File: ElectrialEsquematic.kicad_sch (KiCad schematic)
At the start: 8 parts, among them J1 Conn_01x02_Female, U1 RFM95W-915S2, U3 TP4056, U4 DHT11, U5 NHD-C0220BIZ, U6 L7805

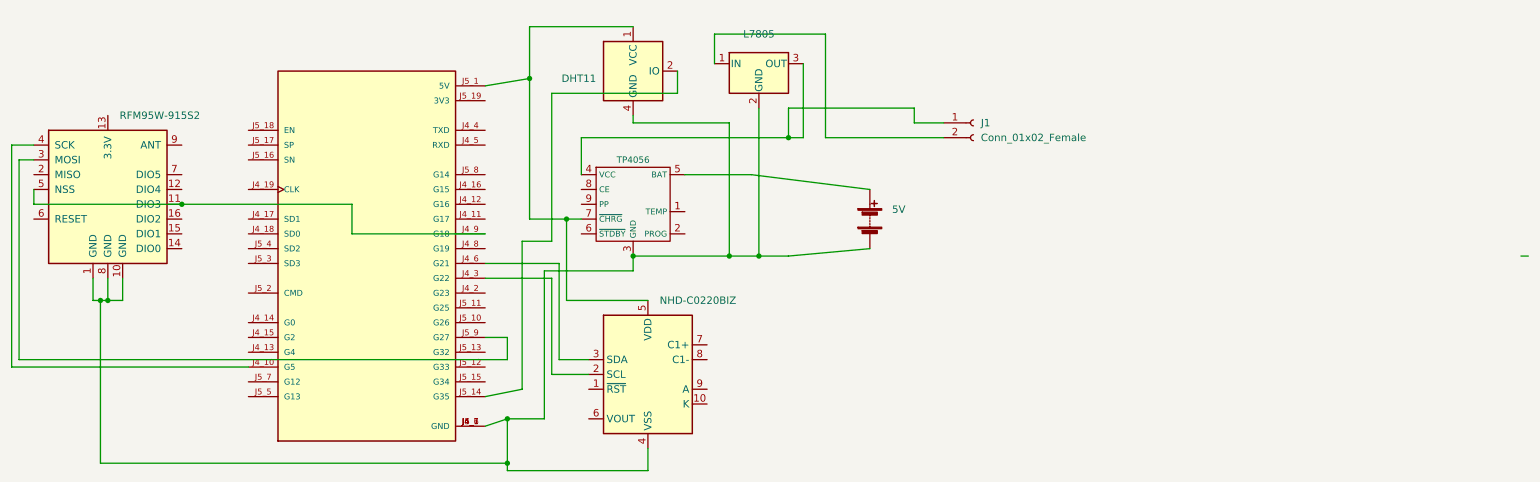
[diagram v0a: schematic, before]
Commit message: Change the Names
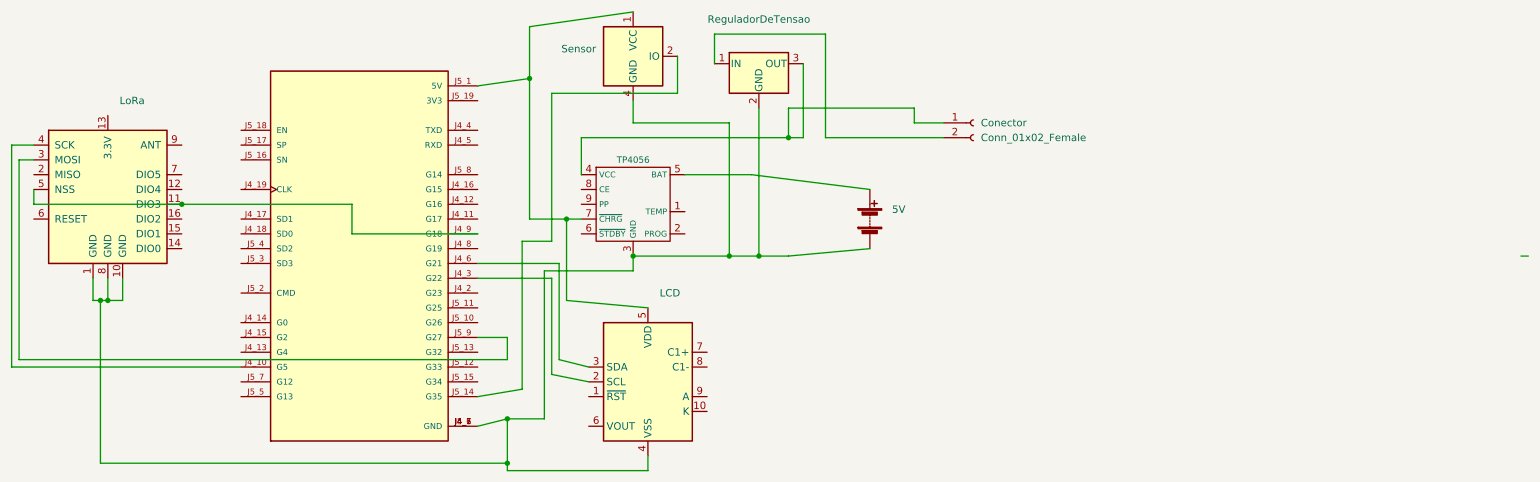
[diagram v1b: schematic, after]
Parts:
- LCD: renamed from U5; value NHD-C0220BIZ -> (none); footprint Display:NHD-C0220BiZ -> (none)
- LoRa: renamed from U1; value RFM95W-915S2 -> (none)
- ReguladorDeTensao: renamed from U6; value L7805 -> (none)
- Sensor: renamed from U4; value DHT11 -> (none); footprint Sensor:Aosong_DHT11_5.5x12.0_P2.54mm -> (none)
- renumbered J1 to Conector

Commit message: ~~
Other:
- company: (none) -> Tractian
- title: (none) -> Esquema Eletrico 
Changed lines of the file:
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@@
 (kicad_sch (version 20211123) (generator eeschema)
   (paper "A4")
+  (title_block
+    (title "Esquema Eletrico ")
+    (rev "05/04/2022")
+    (company "Tractian")
+  )
   (junction (at 139.7 83.82) (diameter 0) (color 0 0 0 0)
   )

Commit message: ~~
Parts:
- 5V: value (none) -> Battery
- LCD: value (none) -> NHD-C0220BIZ; footprint (none) -> Display:NHD-C0220BiZ
- LoRa: value (none) -> RFM95W-915S2
- ReguladorDeTensao: value (none) -> L7805
- Sensor: value (none) -> DHT11; footprint (none) -> Sensor:Aosong_DHT11_5.5x12.0_P2.54mm
- U2: value (none) -> ESP32_NODEMCU; footprint (none) -> MODULE_ESP32_NODEMCU
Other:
- moved on the sheet: Sensor
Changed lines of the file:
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@@
     (stroke (width 0) (type default) (color 0 0 0 0))
   )
-  (wire (pts (xy 158.75 62.23) (xy 158.75 55.88))
+  (wire (pts (xy 158.75 62.23) (xy 158.75 58.42))
     (stroke (width 0) (type default) (color 0 0 0 0))
   )
@@
     (stroke (width 0) (type default) (color 0 0 0 0))
   )
-  (wire (pts (xy 151.13 48.26) (xy 133.35 50.8))
+  (wire (pts (xy 151.13 50.8) (xy 133.35 50.8))
     (stroke (width 0) (type default) (color 0 0 0 0))
   )
@@
     (stroke (width 0) (type default) (color 0 0 0 0))
   )
-  (wire (pts (xy 151.13 67.31) (xy 151.13 63.5))
+  (wire (pts (xy 151.13 67.31) (xy 151.13 66.04))
     (stroke (width 0) (type default) (color 0 0 0 0))
   )
@@
     (stroke (width 0) (type default) (color 0 0 0 0))
   )
-  (symbol (lib_id "Sensor:DHT11") (at 151.13 55.88 0) (unit 1)
-    (in_bom yes) (on_board yes) (fields_autoplaced)
-    (property "Reference" "Sensor" (id 0) (at 144.78 54.6099 0)
+  (symbol (lib_id "Sensor:DHT11") (at 151.13 58.42 0) (unit 1)
+    (in_bom yes) (on_board yes) (fields_autoplaced)
+    (property "Reference" "Sensor" (id 0) (at 144.78 57.1499 0)
       (effects (font (size 1.27 1.27)) (justify right))
     )
-    (property "Value" "" (id 1) (at 144.78 57.1499 0)
+    (property "Value" "DHT11" (id 1) (at 144.78 59.6899 0)
       (effects (font (size 1.27 1.27)) (justify right))
     )
-    (property "Footprint" "" (id 2) (at 151.13 66.04 0)
-      (effects (font (size 1.27 1.27)) hide)
-    )
-    (property "Datasheet" "http://akizukidenshi.com/download/ds/aosong/DHT11.pdf" (id 3) (at 154.94 49.53 0)
+    (property "Footprint" "Sensor:Aosong_DHT11_5.5x12.0_P2.54mm" (id 2) (at 151.13 68.58 0)
+      (effects (font (size 1.27 1.27)) hide)
+    )
+    (property "Datasheet" "http://akizukidenshi.com/download/ds/aosong/DHT11.pdf" (id 3) (at 154.94 52.07 0)
       (effects (font (size 1.27 1.27)) hide)
     )
@@
       (effects (font (size 1.27 1.27)) (justify left))
     )
-    (property "Value" "" (id 1) (at 62.9794 66.04 0)
+    (property "Value" "RFM95W-915S2" (id 1) (at 62.9794 66.04 0)
       (effects (font (size 1.27 1.27)) (justify left))
     )
@@
       (effects (font (size 1.27 1.27)) hide)
     )
-    (property "Value" "" (id 1) (at 104.14 55.88 0))
-    (property "Footprint" "" (id 2) (at 104.14 88.9 0)
+    (property "Value" "ESP32_NODEMCU" (id 1) (at 104.14 55.88 0))
+    (property "Footprint" "MODULE_ESP32_NODEMCU" (id 2) (at 104.14 88.9 0)
       (effects (font (size 1.27 1.27)) (justify left bottom) hide)
     )
@@
       (effects (font (size 1.27 1.27)) (justify left))
     )
-    (property "Value" "" (id 1) (at 155.6894 99.06 0)
-      (effects (font (size 1.27 1.27)) (justify left))
-    )
-    (property "Footprint" "" (id 2) (at 153.67 127 0)
+    (property "Value" "NHD-C0220BIZ" (id 1) (at 155.6894 99.06 0)
+      (effects (font (size 1.27 1.27)) (justify left))
+    )
+    (property "Footprint" "Display:NHD-C0220BiZ" (id 2) (at 153.67 127 0)
       (effects (font (size 1.27 1.27)) hide)
     )
@@
     (in_bom yes) (on_board yes) (fields_autoplaced)
     (property "Reference" "ReguladorDeTensao" (id 0) (at 172.72 49.53 0))
-    (property "Value" "" (id 1) (at 172.72 52.07 0))
+    (property "Value" "L7805" (id 1) (at 172.72 52.07 0))
     (property "Footprint" "" (id 2) (at 173.355 60.96 0)
       (effects (font (size 1.27 1.27) italic) (justify left) hide)
@@
       (effects (font (size 1.27 1.27)) (justify left))
     )
-    (property "Value" "" (id 1) (at 195.58 84.7089 0)
-      (effects (font (size 1.27 1.27)) (justify left))
-    )
+    (property "Value" "Battery" (id 1) (at 195.58 84.7089 0)
+      (effects (font (size 1.27 1.27)) (justify left))
+    )

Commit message: Add Capacitor
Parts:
- added 100n (x3), 10n: (no value), symbol Device:C_Polarized_Small_US
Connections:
- net at LCD.5 (VDD), Sensor.1 (VCC), U2.J5_1 (5V)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: now also 100n.1
- net at 5V.2 (-), LCD.4 (VSS), LoRa.1 (GND)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: now also 100n.2, 10n.2
- net at Conector.1 (Pin_1), U3.4 (VCC): now also 100n.2; no longer ReguladorDeTensao.3 (OUT)
- net at U2.J5_18 (EN): now also 10n.1
- net at Conector.2 (Pin_2): now also 100n.1; no longer ReguladorDeTensao.1 (IN)
- new net: 100n.2, ReguladorDeTensao.1 (IN)
- new net: 100n.1, ReguladorDeTensao.3 (OUT)
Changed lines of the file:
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@@
     (company "Tractian")
   )
+  (junction (at 80.01 125.73) (diameter 0) (color 0 0 0 0)
+  )
   (junction (at 139.7 83.82) (diameter 0) (color 0 0 0 0)
   )
   (junction (at 133.35 59.69) (diameter 0) (color 0 0 0 0)
   )
+  (junction (at 124.46 119.38) (diameter 0) (color 0 0 0 0)
+  )
   (junction (at 60.96 97.79) (diameter 0) (color 0 0 0 0)
   )
   (junction (at 172.72 90.17) (diameter 0) (color 0 0 0 0)
   )
+  (junction (at 124.46 60.96) (diameter 0) (color 0 0 0 0)
+  )
   (junction (at 167.64 90.17) (diameter 0) (color 0 0 0 0)
   )
@@
     (stroke (width 0) (type default) (color 0 0 0 0))
   )
+  (wire (pts (xy 163.83 57.15) (xy 165.1 57.15))
+    (stroke (width 0) (type default) (color 0 0 0 0))
+  )
   (wire (pts (xy 45.72 107.95) (xy 45.72 73.66))
     (stroke (width 0) (type default) (color 0 0 0 0))
   )
-  (wire (pts (xy 180.34 69.85) (xy 180.34 57.15))
-    (stroke (width 0) (type default) (color 0 0 0 0))
-  )
   (wire (pts (xy 138.43 91.44) (xy 124.46 91.44))
     (stroke (width 0) (type default) (color 0 0 0 0))
@@
     (stroke (width 0) (type default) (color 0 0 0 0))
   )
-  (wire (pts (xy 184.15 69.85) (xy 184.15 52.07))
+  (wire (pts (xy 80.01 68.58) (xy 83.82 68.58))
     (stroke (width 0) (type default) (color 0 0 0 0))
   )
@@
     (stroke (width 0) (type default) (color 0 0 0 0))
   )
+  (wire (pts (xy 80.01 73.66) (xy 80.01 125.73))
+    (stroke (width 0) (type default) (color 0 0 0 0))
+  )
+  (wire (pts (xy 184.15 50.8) (xy 161.29 50.8))
+    (stroke (width 0) (type default) (color 0 0 0 0))
+  )
+  (wire (pts (xy 128.27 119.38) (xy 124.46 119.38))
+    (stroke (width 0) (type default) (color 0 0 0 0))
+  )
+  (wire (pts (xy 177.8 69.85) (xy 180.34 69.85))
+    (stroke (width 0) (type default) (color 0 0 0 0))
+  )
   (wire (pts (xy 124.46 86.36) (xy 102.87 86.36))
     (stroke (width 0) (type default) (color 0 0 0 0))
@@
     (stroke (width 0) (type default) (color 0 0 0 0))
   )
-  (wire (pts (xy 129.54 125.73) (xy 59.69 125.73))
+  (wire (pts (xy 129.54 125.73) (xy 80.01 125.73))
     (stroke (width 0) (type default) (color 0 0 0 0))
   )
@@
     (stroke (width 0) (type default) (color 0 0 0 0))
   )
-  (wire (pts (xy 177.8 69.85) (xy 180.34 69.85))
+  (wire (pts (xy 128.27 67.31) (xy 128.27 119.38))
     (stroke (width 0) (type default) (color 0 0 0 0))
   )
@@
     (stroke (width 0) (type default) (color 0 0 0 0))
   )
+  (wire (pts (xy 124.46 62.23) (xy 124.46 60.96))
+    (stroke (width 0) (type default) (color 0 0 0 0))
+  )
   (wire (pts (xy 59.69 97.79) (xy 60.96 97.79))
     (stroke (width 0) (type default) (color 0 0 0 0))
@@
     (stroke (width 0) (type default) (color 0 0 0 0))
   )
+  (wire (pts (xy 161.29 55.88) (xy 163.83 57.15))
+    (stroke (width 0) (type default) (color 0 0 0 0))
+  )
   (wire (pts (xy 153.67 127) (xy 129.54 127))
     (stroke (width 0) (type default) (color 0 0 0 0))
   )
+  (wire (pts (xy 80.01 125.73) (xy 59.69 125.73))
+    (stroke (width 0) (type default) (color 0 0 0 0))
+  )
   (wire (pts (xy 139.7 83.82) (xy 133.35 83.82))
     (stroke (width 0) (type default) (color 0 0 0 0))
@@
     (stroke (width 0) (type default) (color 0 0 0 0))
   )
+  (wire (pts (xy 180.34 63.5) (xy 180.34 69.85))
+    (stroke (width 0) (type default) (color 0 0 0 0))
+  )
   (wire (pts (xy 143.51 109.22) (xy 138.43 107.95))
     (stroke (width 0) (type default) (color 0 0 0 0))
@@
     (stroke (width 0) (type default) (color 0 0 0 0))
   )
-  (wire (pts (xy 184.15 52.07) (xy 165.1 52.07))
-    (stroke (width 0) (type default) (color 0 0 0 0))
-  )
   (wire (pts (xy 199.39 64.77) (xy 177.8 64.77))
     (stroke (width 0) (type default) (color 0 0 0 0))
@@
     (stroke (width 0) (type default) (color 0 0 0 0))
   )
-  (wire (pts (xy 165.1 52.07) (xy 165.1 57.15))
-    (stroke (width 0) (type default) (color 0 0 0 0))
-  )
   (wire (pts (xy 129.54 104.14) (xy 129.54 107.95))
     (stroke (width 0) (type default) (color 0 0 0 0))
@@
     (stroke (width 0) (type default) (color 0 0 0 0))
   )
+  (wire (pts (xy 180.34 57.15) (xy 180.34 58.42))
+    (stroke (width 0) (type default) (color 0 0 0 0))
+  )
   (wire (pts (xy 44.45 109.22) (xy 83.82 109.22))
     (stroke (width 0) (type default) (color 0 0 0 0))
@@
     (stroke (width 0) (type default) (color 0 0 0 0))
   )
+  (wire (pts (xy 128.27 62.23) (xy 124.46 62.23))
+    (stroke (width 0) (type default) (color 0 0 0 0))
+  )
   (wire (pts (xy 153.67 124.46) (xy 153.67 127))
     (stroke (width 0) (type default) (color 0 0 0 0))
@@
   )
   (wire (pts (xy 171.45 76.2) (xy 160.02 76.2))
+    (stroke (width 0) (type default) (color 0 0 0 0))
+  )
+  (wire (pts (xy 184.15 69.85) (xy 184.15 50.8))
     (stroke (width 0) (type default) (color 0 0 0 0))
   )
@@
     (pin "8")
     (pin "9")
+  )
+  (symbol (lib_id "Device:C_Polarized_Small_US") (at 161.29 53.34 0) (unit 1)
+    (in_bom yes) (on_board yes) (fields_autoplaced)
+    (property "Reference" "100n" (id 0) (at 163.83 51.6381 0)
+      (effects (font (size 1.27 1.27)) (justify left))
+    )
+    (property "Value" "" (id 1) (at 163.83 54.1781 0)
+      (effects (font (size 1.27 1.27)) (justify left))
+    )
+    (property "Footprint" "" (id 2) (at 161.29 53.34 0)
+      (effects (font (size 1.27 1.27)) hide)
+    )
+    (property "Datasheet" "~" (id 3) (at 161.29 53.34 0)
+      (effects (font (size 1.27 1.27)) hide)
+    )
+    (pin "1")
+    (pin "2")
   )
   (symbol (lib_id "RF_Module:RFM95W-915S2") (at 60.96 78.74 0) (unit 1)
@@
     (pin "2")
   )
+  (symbol (lib_id "Device:C_Polarized_Small_US") (at 128.27 64.77 0) (unit 1)
+    (in_bom yes) (on_board yes) (fields_autoplaced)
+    (property "Reference" "100n" (id 0) (at 130.81 63.0681 0)
+      (effects (font (size 1.27 1.27)) (justify left))
+    )
+    (property "Value" "" (id 1) (at 130.81 65.6081 0)
+      (effects (font (size 1.27 1.27)) (justify left))
+    )
+    (property "Footprint" "" (id 2) (at 128.27 64.77 0)
+      (effects (font (size 1.27 1.27)) hide)
+    )
+    (property "Datasheet" "~" (id 3) (at 128.27 64.77 0)
+      (effects (font (size 1.27 1.27)) hide)
+    )
+    (pin "1")
+    (pin "2")
+  )
   (symbol (lib_id "Display_Character:NHD-C0220BIZ") (at 153.67 111.76 0) (unit 1)
     (in_bom yes) (on_board yes) (fields_autoplaced)
@@
     (pin "9")
   )
+  (symbol (lib_id "Device:C_Polarized_Small_US") (at 180.34 60.96 0) (unit 1)
+    (in_bom yes) (on_board yes) (fields_autoplaced)
+    (property "Reference" "100n" (id 0) (at 182.88 59.2581 0)
+      (effects (font (size 1.27 1.27)) (justify left))
+    )
+    (property "Value" "" (id 1) (at 182.88 61.7981 0)
+      (effects (font (size 1.27 1.27)) (justify left))
+    )
+    (property "Footprint" "" (id 2) (at 180.34 60.96 0)
+      (effects (font (size 1.27 1.27)) hide)
+    )
+    (property "Datasheet" "~" (id 3) (at 180.34 60.96 0)
+      (effects (font (size 1.27 1.27)) hide)
+    )
+    (pin "1")
+    (pin "2")
+  )
   (symbol (lib_id "Regulator_Linear:L7805") (at 172.72 57.15 0) (unit 1)
     (in_bom yes) (on_board yes) (fields_autoplaced)
@@
     (pin "3")
   )
+  (symbol (lib_id "Device:C_Polarized_Small_US") (at 80.01 71.12 0) (unit 1)
+    (in_bom yes) (on_board yes) (fields_autoplaced)
+    (property "Reference" "10n" (id 0) (at 82.55 69.4181 0)
+      (effects (font (size 1.27 1.27)) (justify left))
+    )
+    (property "Value" "" (id 1) (at 82.55 71.9581 0)
+      (effects (font (size 1.27 1.27)) (justify left))
+    )
+    (property "Footprint" "" (id 2) (at 80.01 71.12 0)
+      (effects (font (size 1.27 1.27)) hide)
+    )
+    (property "Datasheet" "~" (id 3) (at 80.01 71.12 0)
+      (effects (font (size 1.27 1.27)) hide)
+    )
+    (pin "1")
+    (pin "2")
+  )
   (symbol (lib_id "Device:Battery") (at 191.77 83.82 0) (unit 1)
     (in_bom yes) (on_board yes) (fields_autoplaced)
@@
       (reference "5V") (unit 1) (value "Battery") (footprint "")
     )
+    (path "/fa57424c-1a87-42d8-8df8-ed5f102301f4"
+      (reference "10n") (unit 1) (value "Capacitor") (footprint "")
+    )
+    (path "/5e279f2e-23c5-4795-a7c8-145ee445dd00"
+      (reference "100n") (unit 1) (value "Capacitor") (footprint "")
+    )
+    (path "/8c9c2f71-2b7f-4070-8d97-a1f034d62ec9"
+      (reference "100n") (unit 1) (value "Capacitor") (footprint "")
+    )
+    (path "/b769f63b-a3d3-44a7-94e5-34ca824e007d"
+      (reference "100n") (unit 1) (value "Capacitor") (footprint "")
+    )
     (path "/8644b6a1-89d7-44d8-87ac-938fc6afa77b"

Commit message: Arrumando as linhas
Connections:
- net at 100n.2, 10n.2, 5V.2 (-)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: no longer LoRa.1 (GND), LoRa.10 (GND), LoRa.8 (GND)
- new net: LoRa.1 (GND), LoRa.10 (GND), LoRa.8 (GND)
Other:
- moved on the sheet: 10n
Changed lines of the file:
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@@
     (company "Tractian")
   )
-  (junction (at 80.01 125.73) (diameter 0) (color 0 0 0 0)
-  )
   (junction (at 139.7 83.82) (diameter 0) (color 0 0 0 0)
   )
-  (junction (at 133.35 59.69) (diameter 0) (color 0 0 0 0)
-  )
   (junction (at 124.46 119.38) (diameter 0) (color 0 0 0 0)
   )
+  (junction (at 124.46 60.96) (diameter 0) (color 0 0 0 0)
+  )
   (junction (at 60.96 97.79) (diameter 0) (color 0 0 0 0)
   )
   (junction (at 172.72 90.17) (diameter 0) (color 0 0 0 0)
   )
-  (junction (at 124.46 60.96) (diameter 0) (color 0 0 0 0)
+  (junction (at 133.35 50.8) (diameter 0) (color 0 0 0 0)
   )
   (junction (at 167.64 90.17) (diameter 0) (color 0 0 0 0)
@@
     (stroke (width 0) (type default) (color 0 0 0 0))
   )
+  (wire (pts (xy 76.2 125.73) (xy 129.54 125.73))
+    (stroke (width 0) (type default) (color 0 0 0 0))
+  )
+  (wire (pts (xy 124.46 50.8) (xy 124.46 60.96))
+    (stroke (width 0) (type default) (color 0 0 0 0))
+  )
   (wire (pts (xy 129.54 107.95) (xy 45.72 107.95))
     (stroke (width 0) (type default) (color 0 0 0 0))
   )
-  (wire (pts (xy 80.01 68.58) (xy 83.82 68.58))
-    (stroke (width 0) (type default) (color 0 0 0 0))
-  )
   (wire (pts (xy 102.87 86.36) (xy 102.87 81.28))
     (stroke (width 0) (type default) (color 0 0 0 0))
@@
     (stroke (width 0) (type default) (color 0 0 0 0))
   )
-  (wire (pts (xy 80.01 73.66) (xy 80.01 125.73))
-    (stroke (width 0) (type default) (color 0 0 0 0))
-  )
   (wire (pts (xy 184.15 50.8) (xy 161.29 50.8))
     (stroke (width 0) (type default) (color 0 0 0 0))
@@
     (stroke (width 0) (type default) (color 0 0 0 0))
   )
-  (wire (pts (xy 129.54 125.73) (xy 80.01 125.73))
-    (stroke (width 0) (type default) (color 0 0 0 0))
-  )
   (wire (pts (xy 151.13 92.71) (xy 151.13 90.17))
     (stroke (width 0) (type default) (color 0 0 0 0))
   )
-  (wire (pts (xy 133.35 50.8) (xy 133.35 59.69))
-    (stroke (width 0) (type default) (color 0 0 0 0))
-  )
-  (wire (pts (xy 133.35 59.69) (xy 124.46 60.96))
+  (wire (pts (xy 76.2 77.47) (xy 76.2 125.73))
+    (stroke (width 0) (type default) (color 0 0 0 0))
+  )
+  (wire (pts (xy 133.35 50.8) (xy 133.35 83.82))
     (stroke (width 0) (type default) (color 0 0 0 0))
   )
@@
     (stroke (width 0) (type default) (color 0 0 0 0))
   )
+  (wire (pts (xy 133.35 50.8) (xy 124.46 50.8))
+    (stroke (width 0) (type default) (color 0 0 0 0))
+  )
   (wire (pts (xy 153.67 127) (xy 129.54 127))
     (stroke (width 0) (type default) (color 0 0 0 0))
   )
-  (wire (pts (xy 80.01 125.73) (xy 59.69 125.73))
-    (stroke (width 0) (type default) (color 0 0 0 0))
-  )
   (wire (pts (xy 139.7 83.82) (xy 133.35 83.82))
     (stroke (width 0) (type default) (color 0 0 0 0))
@@
     (stroke (width 0) (type default) (color 0 0 0 0))
   )
+  (wire (pts (xy 76.2 68.58) (xy 76.2 72.39))
+    (stroke (width 0) (type default) (color 0 0 0 0))
+  )
   (wire (pts (xy 180.34 63.5) (xy 180.34 69.85))
     (stroke (width 0) (type default) (color 0 0 0 0))
@@
     (stroke (width 0) (type default) (color 0 0 0 0))
   )
-  (wire (pts (xy 133.35 83.82) (xy 133.35 59.69))
+  (wire (pts (xy 83.82 68.58) (xy 76.2 68.58))
     (stroke (width 0) (type default) (color 0 0 0 0))
   )
@@
     (pin "3")
   )
-  (symbol (lib_id "Device:C_Polarized_Small_US") (at 80.01 71.12 0) (unit 1)
-    (in_bom yes) (on_board yes) (fields_autoplaced)
-    (property "Reference" "10n" (id 0) (at 82.55 69.4181 0)
-      (effects (font (size 1.27 1.27)) (justify left))
-    )
-    (property "Value" "" (id 1) (at 82.55 71.9581 0)
-      (effects (font (size 1.27 1.27)) (justify left))
-    )
-    (property "Footprint" "" (id 2) (at 80.01 71.12 0)
-      (effects (font (size 1.27 1.27)) hide)
-    )
-    (property "Datasheet" "~" (id 3) (at 80.01 71.12 0)
-      (effects (font (size 1.27 1.27)) hide)
-    )
+  (symbol (lib_id "Device:C_Polarized_Small_US") (at 76.2 74.93 0) (unit 1)
+    (in_bom yes) (on_board yes) (fields_autoplaced)
+    (property "Reference" "10n" (id 0) (at 78.74 73.2281 0)
+      (effects (font (size 1.27 1.27)) (justify left))
+    )
+    (property "Value" "" (id 1) (at 78.74 75.7681 0)
+      (effects (font (size 1.27 1.27)) (justify left))
+    )
+    (property "Footprint" "" (id 2) (at 76.2 74.93 0)
+      (effects (font (size 1.27 1.27)) hide)
+    )
+    (property "Datasheet" "~" (id 3) (at 76.2 74.93 0)
+      (effects (font (size 1.27 1.27)) hide)
+    )
